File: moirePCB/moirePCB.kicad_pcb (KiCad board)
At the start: 2 copper layers, 38.9 x 152.8 mm, 12 parts, among them J1 Conn_01x13 (Right), J2 Conn_01x13 (Left), U2 OPT3001DNPR, U6 TLC555xD, U7 HDC1080

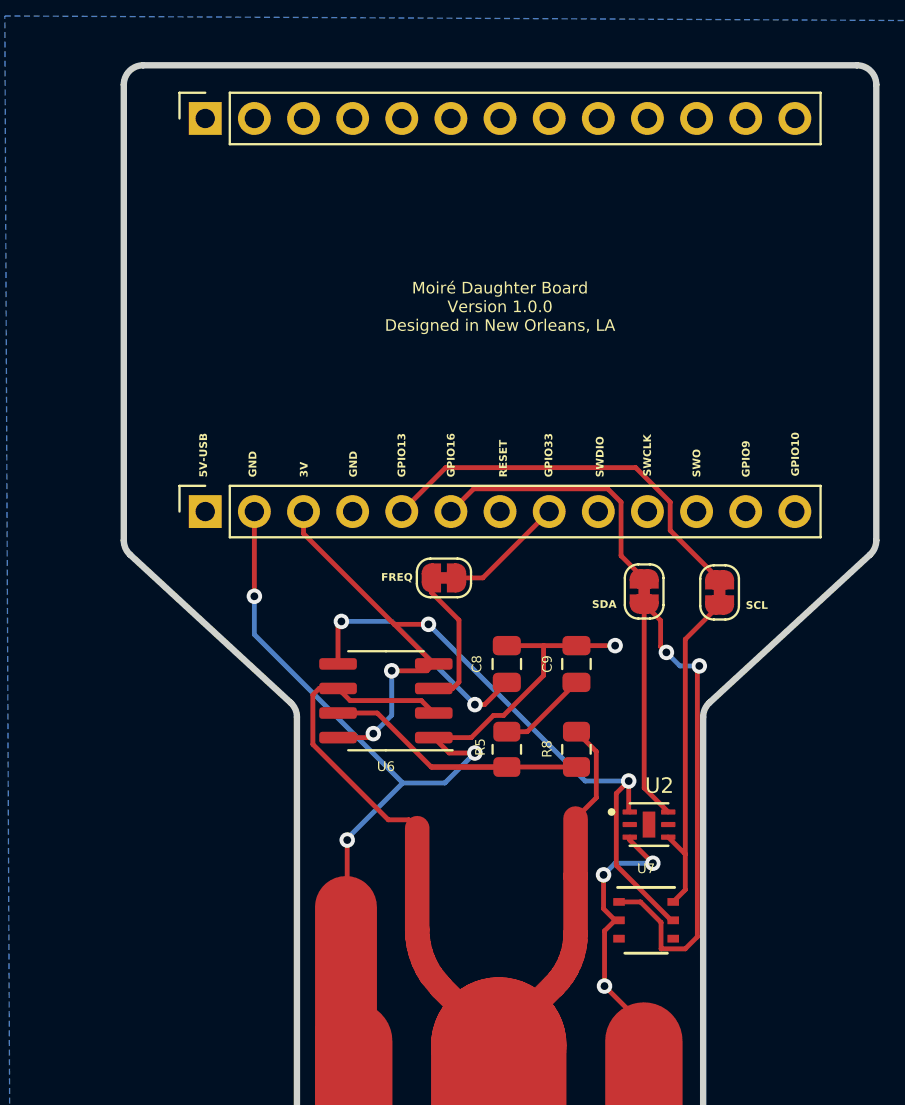
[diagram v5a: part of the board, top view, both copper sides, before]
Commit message: Version 1.0.0 -- moved Helltec board to back, switched i2c sensor location.
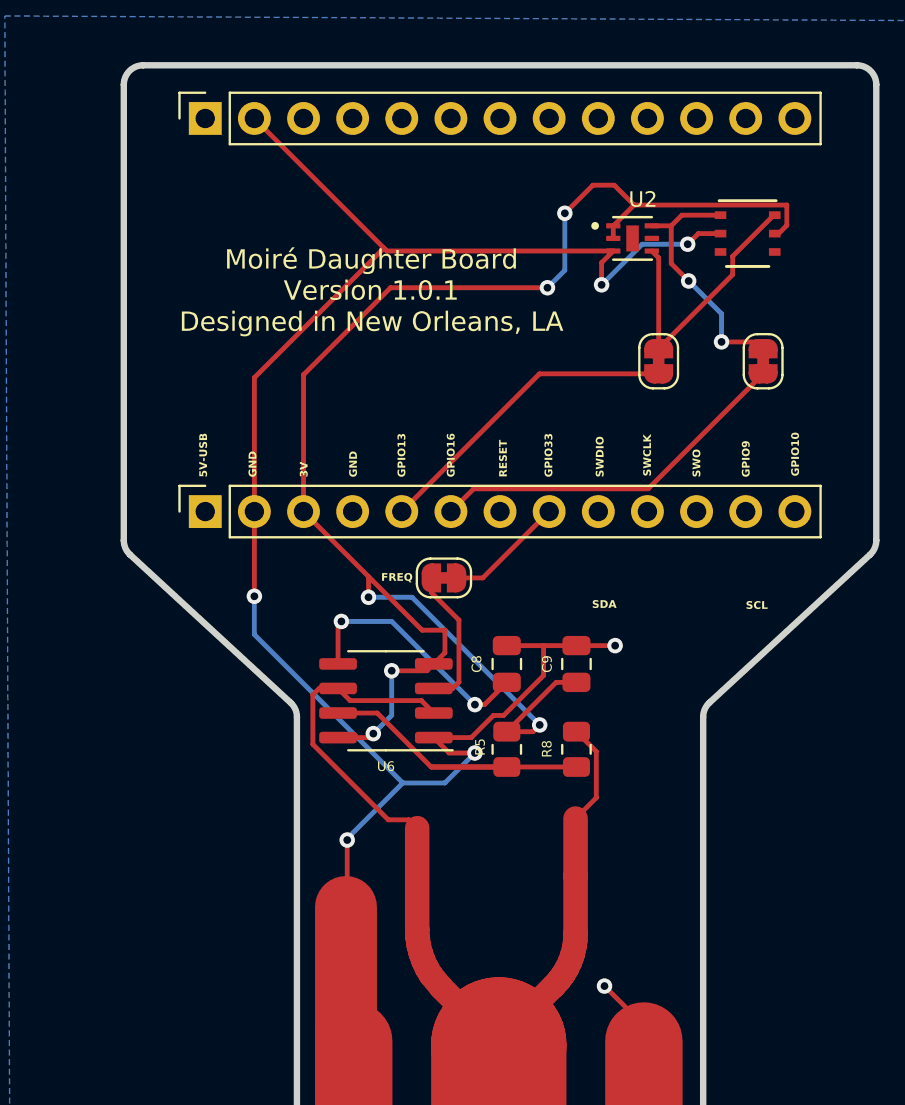
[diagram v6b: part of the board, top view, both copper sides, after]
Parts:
- moved U7 35.9 mm to (163.6, 39.7)
- moved U2 30.3 mm to (157.6, 40.0)
- moved SDA_Jumper1 13.4 mm to (164.3, 46.3), turned to -90 degrees
- moved SCL_Jumper1 12.4 mm to (158.9, 46.3), turned to 90 degrees
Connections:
- J2 pad 2: unconnected-(J2-GND-Pad2) -> GND
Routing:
- net GND: track 307.9 -> 343.8 mm
- net VCC: track 49.0 -> 81.2 mm, vias 4 -> 6
- net Net-(SDA_Jumper1-A): track 36.4 -> 13.2 mm
- net SDA_PIN: track 14.0 -> 19.1 mm
- net SCL_PIN: track 20.6 -> 16.2 mm
- net Net-(SCL_Jumper1-B): track 17.6 -> 14.6 mm
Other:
- board text added: "Moiré Daughter Board Version 1.0.1 Designed in New Orleans, LA"
- board text removed: "Moiré Daughter Board Version 1.0.0 Designed in New Orleans, LA"
